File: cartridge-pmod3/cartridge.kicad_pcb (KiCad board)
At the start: 2 copper layers, 64.8 x 60.3 mm, 31 parts, among them J1 Cartridge Connector, U1 S70KL1281-pkl_memory, U2 W25Q128, U3 AP2112K-3.3, U4 AP2112K-3.3, U5 AP2112K-3.3

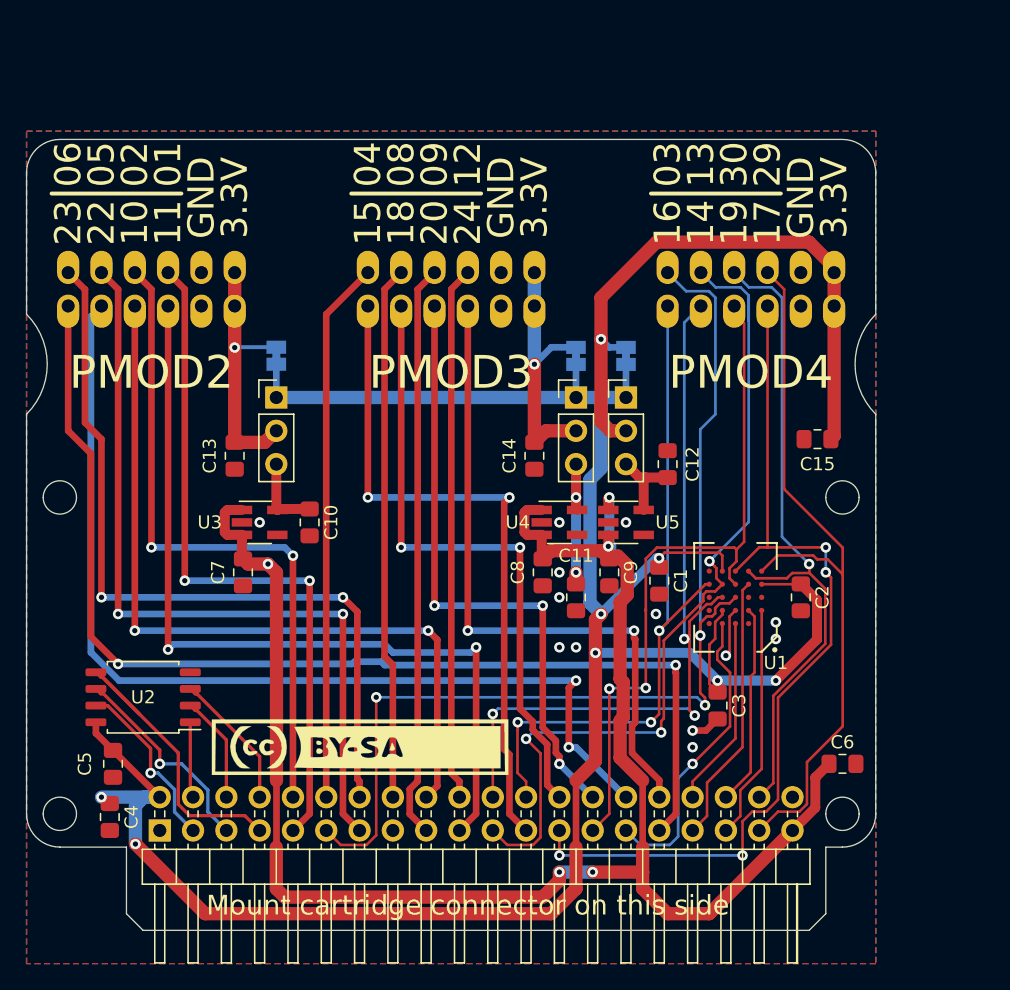
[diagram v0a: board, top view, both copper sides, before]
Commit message: pmod3-cartridge: rev  1.1 - fix 2x20 pinout, add 1x9, remove 3.3v supplies
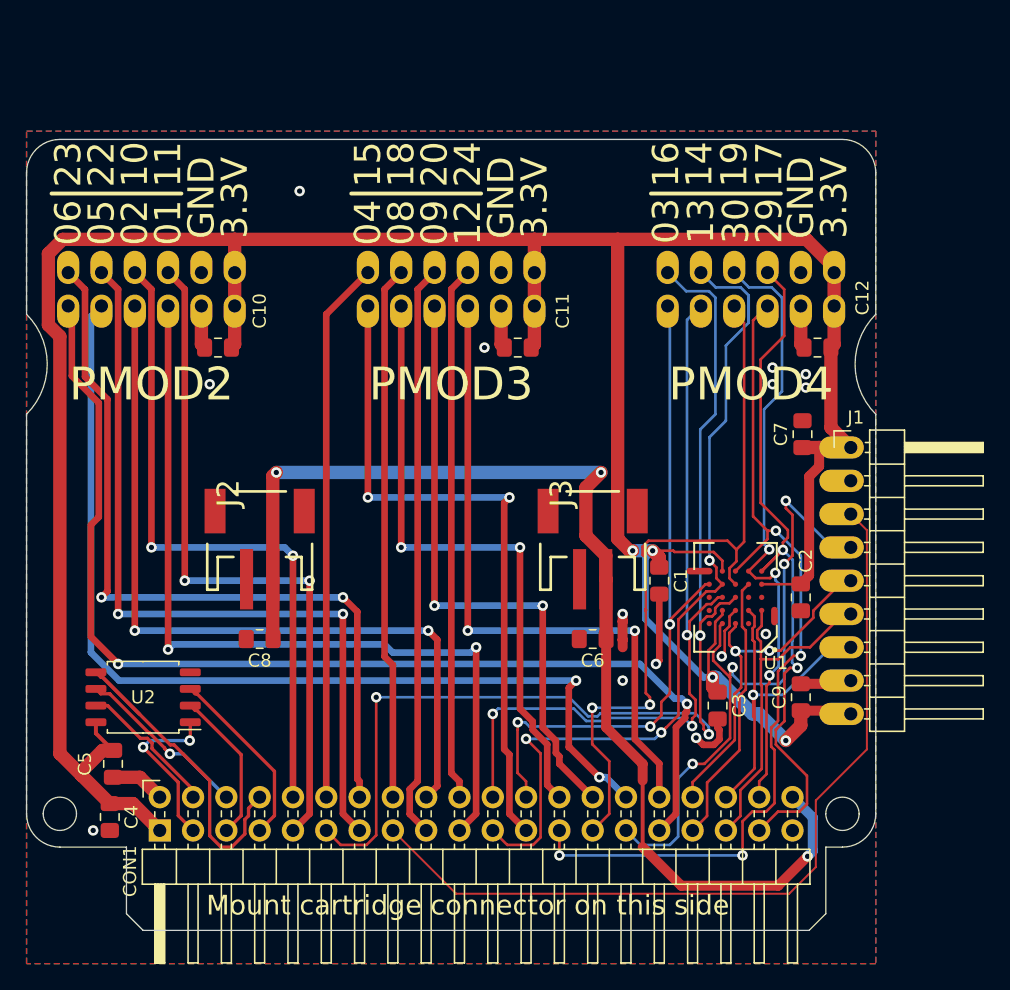
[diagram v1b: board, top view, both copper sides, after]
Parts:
- removed the C10 at (88.9, 73.0)
- removed the C11 at (109.2, 78.7)
- removed the C12 at (116.2, 68.6)
- removed G***: LOGO, tom-mechanical:cc-by-sa-80x15
- removed JP1, JP2, JP3: JUMPER3, tom-connectors:PinHeader_1x03_P2.54mm_Vertical
- removed JP4, JP5, JP6: JUMPER, tom-mechanical:SolderJumper-2_P1.3mm_Bridged_Pad1.0x1.5mm
- removed U3, U4, U5: AP2112K-3.3, tom-semiconductors:SOT-23-5_HandSoldering
- added CON1: Conn_02x20_Odd_Even, tom-connectors:PinHeader_2x20_P2.54mm_Horizontal_Mirrored, F.Cu at (77.5, 96.5)
- added J2: Conn_01x02, tom-connectors:JST-2-SMD, F.Cu at (85.1, 73.7)
- added J3: Conn_01x02, tom-connectors:JST-2-SMD, F.Cu at (110.5, 73.7)
- C6: value 10uF/10V -> 10uF
- C7, C8, C9: value 1uF/10V -> 10uF
- J1: value Cartridge Connector -> Conn_01x09_Male; footprint SuperconCartridge:Supercon_Cartridge_40pin_Connector -> tom-connectors:PinHeader_1x09_P2.54mm_Horizontal
- moved C7 44.0 mm to (126.5, 66.3), turned to 90 degrees
- moved J1 27.0 mm to (130.2, 67.3), turned to 0 degrees
- moved C8 22.2 mm to (85.1, 81.9), turned to 180 degrees
- moved C6 21.3 mm to (110.5, 81.9), turned to 180 degrees
- moved C9 17.4 mm to (126.4, 86.4), turned to 90 degrees
- moved C10 8.35 mm to (81.9, 59.7), turned to 180 degrees
- moved C11 8.35 mm to (104.8, 59.7), turned to 180 degrees
- moved C12 6.98 mm to (127.6, 59.7)
- renumbered C13 to C10, C14 to C11, C15 to C12
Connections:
- C10 pad 1: /3V3-PMOD2 -> +3V3
- C11 pad 1: /3V3-PMOD3 -> +3V3
- C12 pad 1: /3V3-PMOD4 -> +3V3
- C7 pad 1: +5V -> +3V3
- C9 pad 1: +5V -> +3V3
- J1 pad 1: GND -> +3V3
- J1 pad 2: +3V3 -> GND
- J1 pad 3: F_HOLD -> GENIO7_PT6B
- J1 pad 4: F_CS -> GENIO21_PT42A
- J1 pad 5: F_SCK -> GENIO26_PR20B
- J1 pad 6: F_MISO -> GENIO27_PT44A
- J1 pad 7: F_MOSI -> GENIO28_PT49A
- J1 pad 8: F_WP -> GND
- J1 pad 9: GENIO1_PL11D_N -> +3V3
- PMOD2 pad 12: /3V3-PMOD2 -> +3V3
- PMOD2 pad 6: /3V3-PMOD2 -> +3V3
- PMOD3 pad 12: /3V3-PMOD3 -> +3V3
- PMOD3 pad 6: /3V3-PMOD3 -> +3V3
- PMOD4 pad 12: /3V3-PMOD4 -> +3V3
- PMOD4 pad 6: /3V3-PMOD4 -> +3V3
- U2 pad 1: F_CS -> CS
- U2 pad 2: F_MISO -> MISO
- U2 pad 3: F_WP -> WP
- U2 pad 5: F_MOSI -> MOSI
- U2 pad 6: F_SCK -> SCK
- U2 pad 7: F_HOLD -> HOLD
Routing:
- net GENIO7_PT6B: track 0.00 -> 64.1 mm
- net +3V3: track 174.7 -> 233.2 mm, vias 7 -> 4
- net /3V3-PMOD4: track 46.8 -> 0.00 mm, vias 1 -> 0
- net +5V: track 129.0 -> 88.5 mm, vias 5 -> 3
- net GND: track 6.41 -> 36.5 mm, vias 13 -> 14
- net GENIO21_PT42A: track 23.1 -> 50.2 mm, vias 1 -> 4
- net MOSI: track 0.00 -> 27.0 mm
- net F_MOSI: track 23.8 -> 0.00 mm
- net /3V3-PMOD3: track 20.2 -> 0.00 mm, vias 1 -> 0
- net /3V3-PMOD2: track 19.7 -> 0.00 mm, vias 1 -> 0
- net F_SCK: track 16.0 -> 0.00 mm, vias 1 -> 0
- net WP: track 0.00 -> 14.0 mm
- net F_HOLD: track 13.5 -> 0.00 mm, vias 1 -> 0
- net SCK: track 0.00 -> 13.4 mm, vias 0 -> 1
- net CS: track 0.00 -> 13.1 mm, vias 0 -> 2
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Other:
- outline, holes or cut-outs redrawn
- board text added: "3.3V GND 7 21 26 27 28 GND 3.3V"
- board text added: "@TomKeddie v1.1"
- board text added: "pmod3.tomk.in"
- board text removed: "tom@tomk.in v1.0"

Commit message: pmod3-cartridge: v1.2 larger board to reveal silk above badge
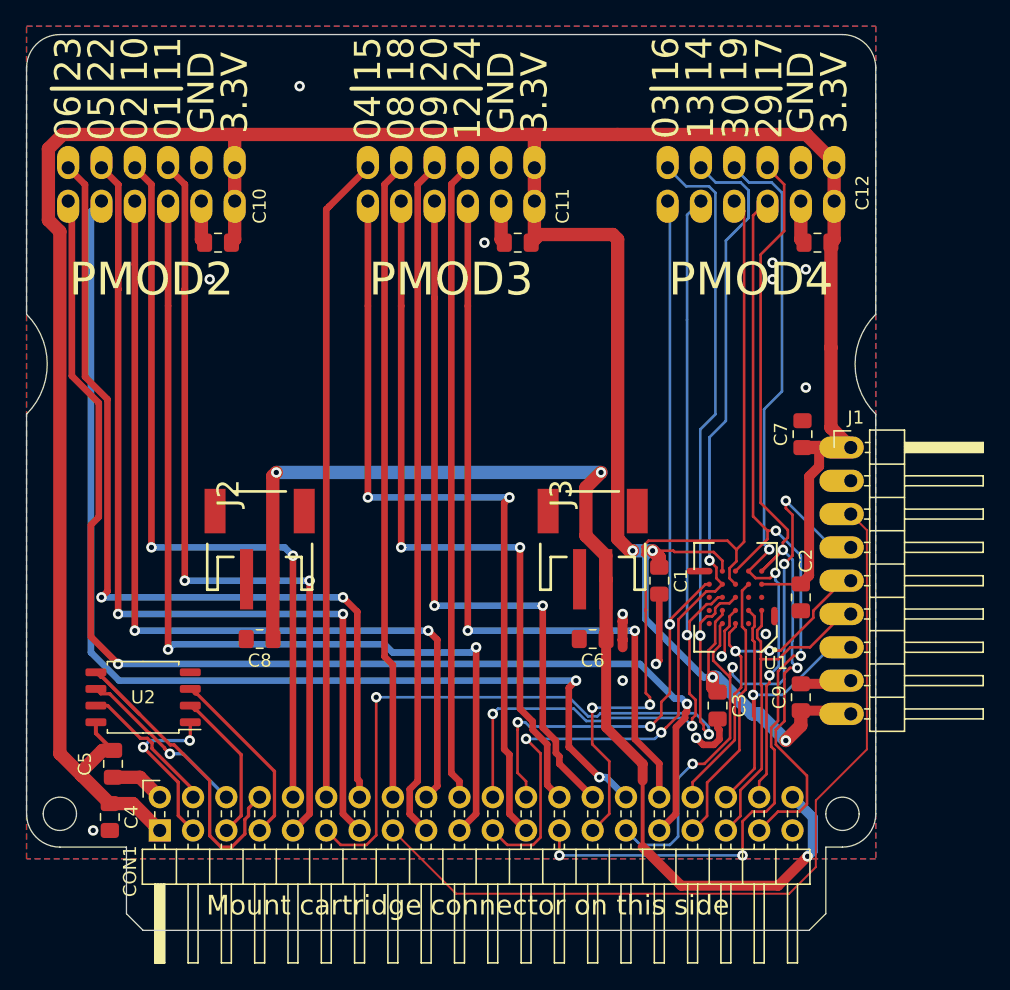
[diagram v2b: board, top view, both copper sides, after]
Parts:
- moved C10 8.00 mm to (81.9, 51.7)
- moved C11 8.00 mm to (104.8, 51.7)
- moved C12 8.00 mm to (127.6, 51.7)
- moved PMOD2 8.00 mm to (76.8, 47.2)
- moved PMOD3 8.00 mm to (99.7, 47.2)
- moved PMOD4 8.00 mm to (122.6, 47.2)
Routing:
- net +3V3: track 233.2 -> 256.2 mm
- net GENIO19_PT33B: track 55.6 -> 65.2 mm
- net GENIO5_PT4B_N: track 60.7 -> 68.8 mm
- net GENIO1_PL11D_N: track 53.1 -> 61.1 mm
- net GENIO6_PT4A_P: track 60.4 -> 68.4 mm
- net GENIO9_PT18A_P: track 43.9 -> 51.9 mm
- net GENIO8_PT11B_N: track 40.8 -> 48.8 mm
- net GENIO4_PT11A_P: track 41.3 -> 49.3 mm
- net GENIO3_PL11B: track 85.3 -> 93.3 mm
- net GENIO30_PT56B: track 46.9 -> 54.9 mm
- net GENIO2_PL11C_P: track 51.0 -> 59.0 mm
- net GENIO29_PR14B: track 53.8 -> 61.8 mm
- net GENIO24_PT36B_N: track 51.0 -> 59.0 mm
- net GENIO23_PT38A_P: track 84.6 -> 92.6 mm
- net GENIO22_PT38B_N: track 75.9 -> 83.9 mm
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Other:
- board size 64.8 x 60.3 mm -> 64.8 x 68.3 mm
- board text added: "@TomKeddie v1.2"
- board text removed: "@TomKeddie v1.1"

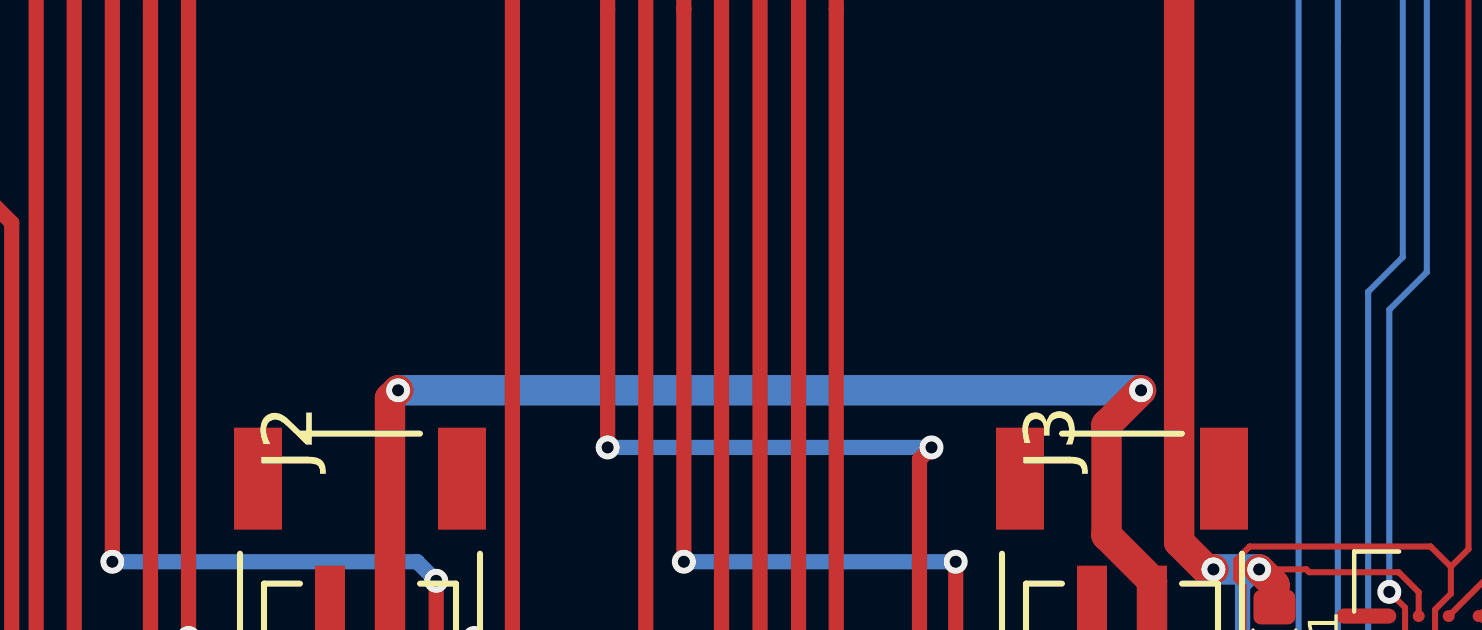
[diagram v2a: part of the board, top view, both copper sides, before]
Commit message: pmod3-cartridge: updated for v1.2
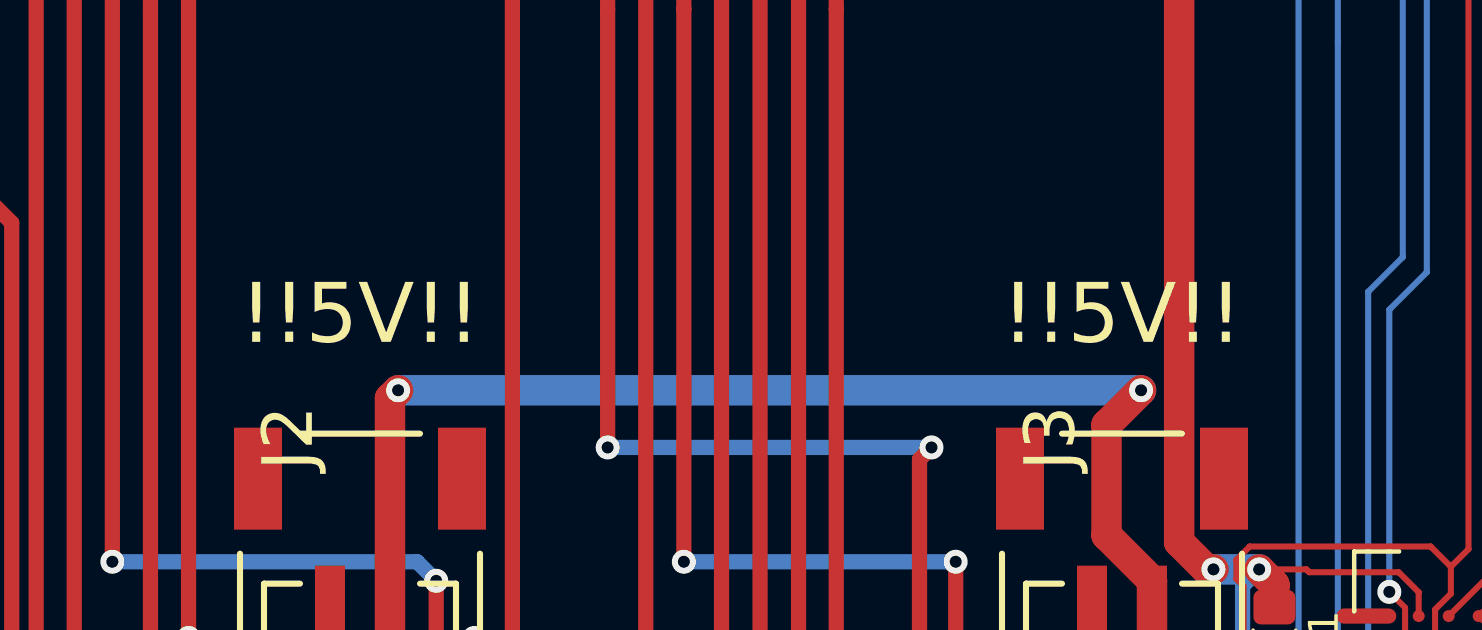
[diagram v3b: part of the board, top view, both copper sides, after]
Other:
- board text added: "!!5V!!"
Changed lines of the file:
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@@
   (general
     (thickness 1.6)
-    (drawings 75)
+    (drawings 77)
     (tracks 654)
     (zones 0)
@@
   (page A4)
   (layers
-    (0 F.Cu signal hide)
+    (0 F.Cu signal)
     (31 B.Cu signal)
     (32 B.Adhes user)
@@
     (pcbplotparams
       (layerselection 0x010fc_ffffffff)
-      (usegerberextensions true)
+      (usegerberextensions false)
       (usegerberattributes false)
       (usegerberadvancedattributes false)
@@
     )
   )
+  (gr_text !!5V!! (at 110.49 66.675) (layer F.SilkS)
+    (effects (font (size 2 2) (thickness 0.4)))
+  )
+  (gr_text !!5V!! (at 85.09 66.675) (layer F.SilkS)
+    (effects (font (size 2 2) (thickness 0.4)))
+  )
   (gr_line (start 132.08 49.15) (end 132.08 57.150002) (layer Edge.Cuts) (width 0.05))
   (gr_line (start 67.31 49.15) (end 67.31 57.15) (layer Edge.Cuts) (width 0.05))
@@
   )
   (gr_line (start 69.85 35.815) (end 129.54 35.815) (layer Edge.Cuts) (width 0.05))
-  (gr_text 3 (at 71.628 68.834) (layer B.SilkS)
+  (gr_text 3 (at 73.7743 69.5706) (layer B.SilkS)
     (effects (font (size 8 8) (thickness 2)) (justify mirror))
   )
-  (gr_text PMOD (at 93.726 82.804) (layer B.SilkS)
+  (gr_text PMOD (at 99.6442 82.7786) (layer B.SilkS)
     (effects (font (size 14 12) (thickness 2.8)) (justify mirror))
   )
